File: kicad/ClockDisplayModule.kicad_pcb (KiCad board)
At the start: 2 copper layers, 91.4 x 58.4 mm, 44 parts, among them IC1 ATMEGA88PA-A, P101 CONN_02X03, P102 CONN_01X05, P201 CONN_01X06, P202 CONN_01X07, P203 CONN_01X06, P204 CONN_01X07, Q201 BC856BS, Q202 BC856BS, Q203 BC856BS, U201 SN74LS138, U202 74HC4511

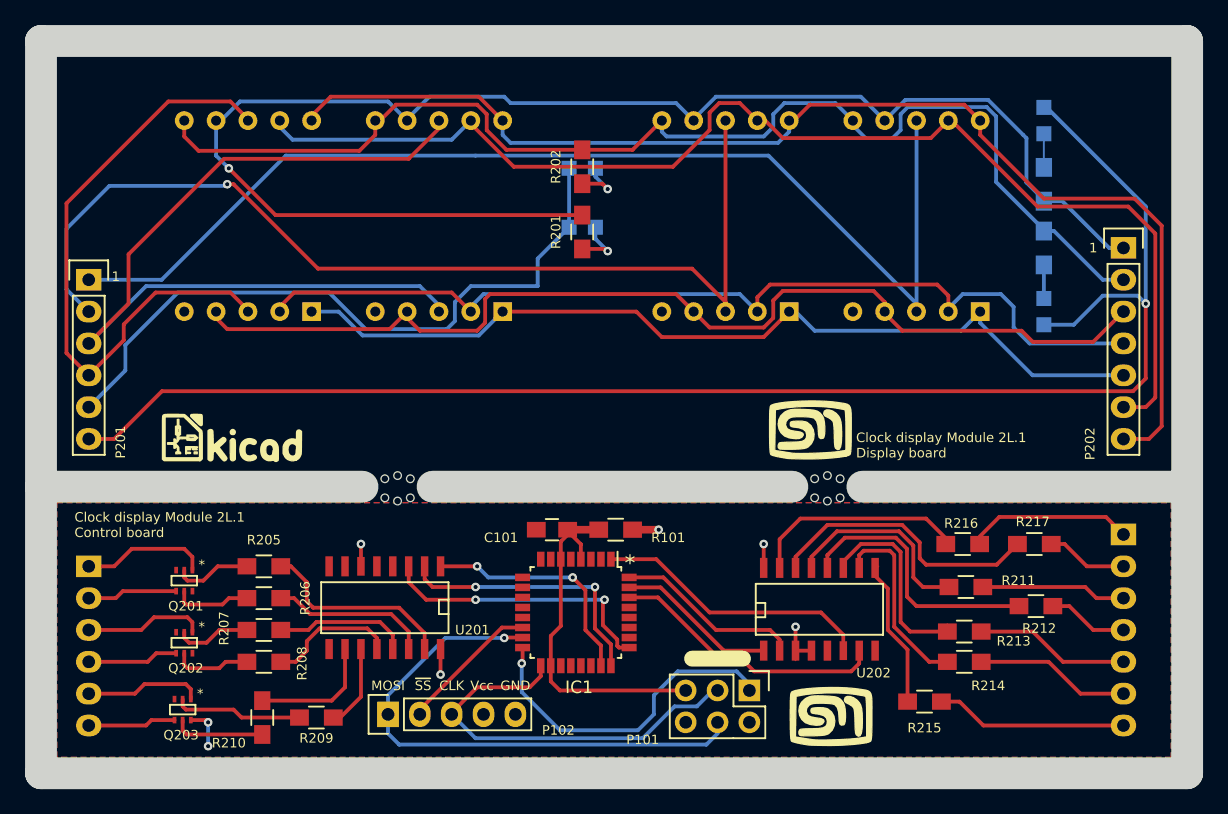
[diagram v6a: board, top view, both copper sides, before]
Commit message: Updated main project with fixes from issues discovered when brining up the board
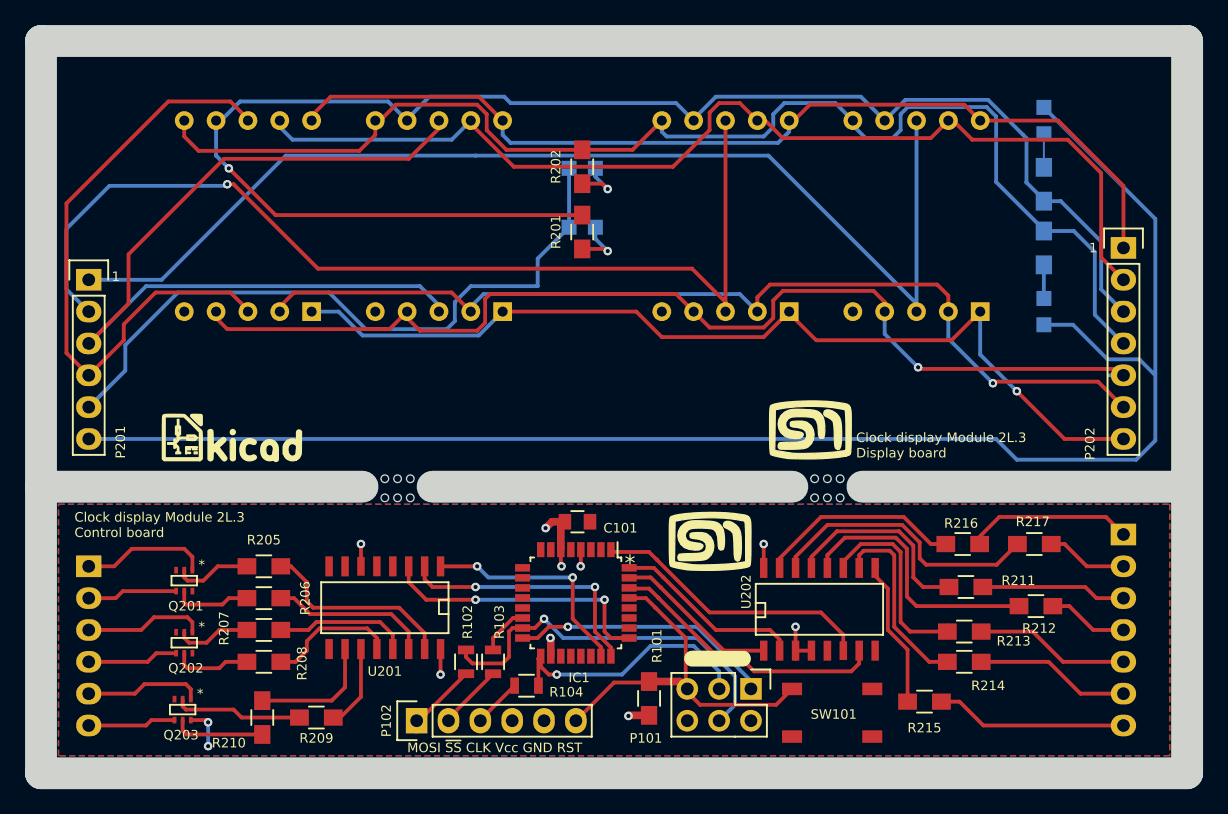
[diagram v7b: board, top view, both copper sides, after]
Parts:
- added R102: 1K, Resistors_SMD:R_0805, F.Cu at (149.5, 91.4)
- added R103: 1K, Resistors_SMD:R_0805, F.Cu at (151.6, 91.4)
- added R104: 1K, Resistors_SMD:R_0805, F.Cu at (154.3, 93.3)
- added SW101: SW_PUSH, ClockFootprints:PTS525SM15SMTR2LFS, F.Cu at (178.7, 95.5)
- C101: footprint Capacitors_SMD:C_0805_HandSoldering -> Capacitors_SMD:C_0805
- P102: value CONN_01X05 -> CONN_01X06; footprint Pin_Headers:Pin_Header_Straight_1x05 -> Pin_Headers:Pin_Header_Straight_1x06
- moved G*** 17.0 mm to (168.9, 81.8)
- moved R101 13.7 mm to (164.1, 94.4), turned to 90 degrees
- moved P102 2.34 mm to (145.5, 96.1)
- moved C101 2.13 mm to (158.4, 80.3), turned to 0 degrees
- moved IC1 0.76 mm to (158.2, 86.7)
- moved P101 0.18 mm to (172.2, 93.6)
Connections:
- AFF201 pad 5: (no net) -> Net-(AFF201-Pad5)
- AFF202 pad 5: (no net) -> Net-(AFF202-Pad5)
- AFF203 pad 5: (no net) -> Net-(AFF203-Pad5)
- AFF204 pad 5: (no net) -> Net-(AFF204-Pad5)
- C101 pad 1: Reset -> VCC
- IC1 pad 10: (no net) -> Net-(IC1-Pad10)
- IC1 pad 11: (no net) -> Net-(IC1-Pad11)
- IC1 pad 12: (no net) -> Net-(IC1-Pad12)
- IC1 pad 13: (no net) -> Net-(IC1-Pad13)
- IC1 pad 18: Reset -> VCC
- IC1 pad 19: (no net) -> Net-(IC1-Pad19)
- IC1 pad 2: (no net) -> Net-(IC1-Pad2)
- IC1 pad 20: (no net) -> Net-(IC1-Pad20)
- IC1 pad 22: (no net) -> Net-(IC1-Pad22)
- IC1 pad 26: (no net) -> Net-(IC1-Pad26)
- IC1 pad 27: (no net) -> Net-(IC1-Pad27)
- IC1 pad 28: (no net) -> Net-(IC1-Pad28)
- IC1 pad 29: (no net) -> Reset
- IC1 pad 4: Reset -> VCC
- IC1 pad 6: Reset -> VCC
- IC1 pad 7: (no net) -> Net-(IC1-Pad7)
- IC1 pad 8: (no net) -> Net-(IC1-Pad8)
- IC1 pad 9: (no net) -> Net-(IC1-Pad9)
- P102 pad 1: MOSI -> Net-(P102-Pad1)
- P102 pad 2: ~SS -> Net-(P102-Pad2)
- P102 pad 3: CLK -> Net-(P102-Pad3)
- P202 pad 1: /Display Driver/Seg_A -> /Display Driver/Seg_G
- P202 pad 2: /Display Driver/Seg_B -> /Display Driver/Seg_F
- P202 pad 3: /Display Driver/Seg_C -> /Display Driver/Seg_A
- P202 pad 4: /Display Driver/Seg_D -> /Display Driver/Seg_B
- P202 pad 5: /Display Driver/Seg_E -> /Display Driver/Seg_C
- P202 pad 6: /Display Driver/Seg_F -> /Display Driver/Seg_D
- P202 pad 7: /Display Driver/Seg_G -> /Display Driver/Seg_E
- R101 pad 1: Reset -> VCC
- R101 pad 2: VCC -> Reset
- U201 pad 7: (no net) -> Net-(U201-Pad7)
- U201 pad 9: (no net) -> Net-(U201-Pad9)
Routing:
- net /Display Driver/Seg_G: track 98.9 -> 79.3 mm
- net MOSI: track 44.2 -> 30.9 mm
- net /Display Driver/Seg_F: track 98.8 -> 86.1 mm
- net CLK: track 32.9 -> 21.3 mm, vias 0 -> 1
- net VCC: track 11.7 -> 19.6 mm, vias 5 -> 9
- net ~SS: track 11.4 -> 3.97 mm
- net D_Signal: track 120.8 -> 127.4 mm, vias 1 -> 0
- net Net-(P102-Pad1): track 0.00 -> 6.51 mm
- net Net-(P102-Pad2): track 0.00 -> 6.18 mm
- net MISO: track 26.8 -> 21.6 mm
- net /Display Driver/Seg_B: track 97.7 -> 102.7 mm
- net /Display Driver/Seg_E: track 72.6 -> 77.5 mm, vias 0 -> 1
- net /Display Driver/Seg_A: track 120.0 -> 124.5 mm
- net Net-(P102-Pad3): track 0.00 -> 3.93 mm
- net /Display Driver/Seg_C: track 84.0 -> 86.2 mm, vias 0 -> 1
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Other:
- board text added: "Clock display Module 2L.3 Control board"
- board text added: "Clock display Module 2L.3 Display board"
- board text added: "MOSI ~SS~ CLK Vcc GND RST"
- board text removed: "CLK"
- board text removed: "Clock display Module 2L.1 Control board"
- board text removed: "Clock display Module 2L.1 Display board"
- board text removed: "GND"
- board text removed: "MOSI"
- board text removed: "Vcc"
- board text removed: "~SS"
